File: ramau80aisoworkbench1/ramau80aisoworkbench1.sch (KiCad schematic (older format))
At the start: 190 parts, among them SW1 SW_PUSH, U1 ATmega32U4-AU, Y1 16MHz

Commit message: label updates
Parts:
- gave numbers to parts that had none: 13
- renumbered C6 to C1, C5 to C2, C4 to C3, C1 to C4, C2 to C5, C3 to C6, D_BKSP to D_BKSP1, D_EQ to D_EQ1, D_MIN to D_MIN1, MX_BKSP to MX_BKSP1, MX_EQ to MX_EQ1, MX_MIN to MX_MIN1
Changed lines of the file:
@@
 $EndComp
 $Comp
-L Device:C_Small C6
+L Device:C_Small C1
 U 1 1 6413AAB8
 P 2700 5600
-F 0 "C6" H 2792 5646 50  0000 L CNN
+F 0 "C1" H 2792 5646 50  0000 L CNN
 F 1 "C_Small" H 2792 5555 50  0000 L CNN
 F 2 "Capacitor_SMD:C_0805_2012Metric" H 2700 5600 50  0001 C CNN
@@
 	3650 5750 3650 5550
 $Comp
-L Device:C_Small C4
+L Device:C_Small C3
 U 1 1 64154BDF
 P 4000 5250
-F 0 "C4" V 3771 5250 50  0000 C CNN
+F 0 "C3" V 3771 5250 50  0000 C CNN
 F 1 "22pF" V 3862 5250 50  0000 C CNN
 F 2 "Capacitor_SMD:C_0805_2012Metric" H 4000 5250 50  0001 C CNN
@@
 $EndComp
 $Comp
-L Device:C_Small C5
+L Device:C_Small C2
 U 1 1 6415BB1E
 P 3650 5250
-F 0 "C5" V 3421 5250 50  0000 C CNN
+F 0 "C2" V 3421 5250 50  0000 C CNN
 F 1 "22pF" V 3512 5250 50  0000 C CNN
 F 2 "Capacitor_SMD:C_0805_2012Metric" H 3650 5250 50  0001 C CNN
@@
 $EndComp
 $Comp
-L Device:D_Small D_F?
+L Device:D_Small D_F13
 U 1 1 641E009B
 P 8750 1450
-F 0 "D_F?" V 8796 1380 50  0000 R CNN
+F 0 "D_F13" V 8796 1380 50  0000 R CNN
 F 1 "D_Small" V 8705 1380 50  0000 R CNN
 F 2 "Diode_SMD:D_SOD-123" V 8750 1450 50  0001 C CNN
@@
 $EndComp
 $Comp
-L Device:D_Small D_F?
+L Device:D_Small D_F14
 U 1 1 641E0688
 P 9250 1450
-F 0 "D_F?" V 9296 1380 50  0000 R CNN
+F 0 "D_F14" V 9296 1380 50  0000 R CNN
 F 1 "D_Small" V 9205 1380 50  0000 R CNN
 F 2 "Diode_SMD:D_SOD-123" V 9250 1450 50  0001 C CNN
@@
 $EndComp
 $Comp
-L Device:D_Small D_F?
+L Device:D_Small D_F15
 U 1 1 641E0B3F
 P 9750 1450
-F 0 "D_F?" V 9796 1380 50  0000 R CNN
+F 0 "D_F15" V 9796 1380 50  0000 R CNN
 F 1 "D_Small" V 9705 1380 50  0000 R CNN
 F 2 "Diode_SMD:D_SOD-123" V 9750 1450 50  0001 C CNN
@@
 Wire Wire Line
 	1250 1950 1450 1950
-$Comp
-L MX_Alps_Hybrid:MX-NoLED MX_GRV
-U 1 1 64185B4E
-P 1500 1800
-F 0 "MX_GRV" H 1533 2023 60  0000 C CNN
-F 1 "MX-NoLED" H 1533 1949 20  0000 C CNN
-F 2 "MX_Only:MXOnly-1U" H 875 1775 60  0001 C CNN
-F 3 "" H 875 1775 60  0001 C CNN
-	1    1500 1800
-	1    0    0    -1
-$EndComp
 Wire Wire Line
 	1650 1150 1650 900
@@
 $EndComp
 $Comp
-L MX_Alps_Hybrid:MX-NoLED MX_MIN
+L MX_Alps_Hybrid:MX-NoLED MX_MIN1
 U 1 1 642DE91B
 P 7000 1800
-F 0 "MX_MIN" H 7033 2023 60  0000 C CNN
+F 0 "MX_MIN1" H 7033 2023 60  0000 C CNN
 F 1 "MX-NoLED" H 7033 1949 20  0000 C CNN
 F 2 "MX_Only:MXOnly-1U" H 6375 1775 60  0001 C CNN
@@
 $EndComp
 $Comp
-L MX_Alps_Hybrid:MX-NoLED MX_EQ
+L MX_Alps_Hybrid:MX-NoLED MX_EQ1
 U 1 1 642DE925
 P 7500 1800
-F 0 "MX_EQ" H 7533 2023 60  0000 C CNN
+F 0 "MX_EQ1" H 7533 2023 60  0000 C CNN
 F 1 "MX-NoLED" H 7533 1949 20  0000 C CNN
 F 2 "MX_Only:MXOnly-1U" H 6875 1775 60  0001 C CNN
@@
 $EndComp
 $Comp
-L MX_Alps_Hybrid:MX-NoLED MX_BKSP
+L MX_Alps_Hybrid:MX-NoLED MX_BKSP1
 U 1 1 642DE92F
 P 8100 1800
-F 0 "MX_BKSP" H 8133 2023 60  0000 C CNN
+F 0 "MX_BKSP1" H 8133 2023 60  0000 C CNN
 F 1 "MX-NoLED" H 8133 1949 20  0000 C CNN
 F 2 "MX_Only:MXOnly-1U" H 7475 1775 60  0001 C CNN
@@
 $EndComp
 $Comp
-L Device:D_Small D_MIN
+L Device:D_Small D_MIN1
 U 1 1 642DE99D
 P 6750 2050
-F 0 "D_MIN" V 6796 1980 50  0000 R CNN
+F 0 "D_MIN1" V 6796 1980 50  0000 R CNN
 F 1 "D_Small" V 6705 1980 50  0000 R CNN
 F 2 "Diode_SMD:D_SOD-123" V 6750 2050 50  0001 C CNN
@@
 $EndComp
 $Comp
-L Device:D_Small D_EQ
+L Device:D_Small D_EQ1
 U 1 1 642DE9A7
 P 7250 2050
-F 0 "D_EQ" V 7296 1980 50  0000 R CNN
+F 0 "D_EQ1" V 7296 1980 50  0000 R CNN
 F 1 "D_Small" V 7205 1980 50  0000 R CNN
 F 2 "Diode_SMD:D_SOD-123" V 7250 2050 50  0001 C CNN
@@
 $EndComp
 $Comp
-L Device:D_Small D_BKSP
+L Device:D_Small D_BKSP1
 U 1 1 642DE9B1
 P 7850 2050
-F 0 "D_BKSP" V 7896 1980 50  0000 R CNN
+F 0 "D_BKSP1" V 7896 1980 50  0000 R CNN
 F 1 "D_Small" V 7805 1980 50  0000 R CNN
 F 2 "Diode_SMD:D_SOD-123" V 7850 2050 50  0001 C CNN
@@
 	2750 1350 2950 1350
 $Comp
-L Device:D_Small D_F?
+L Device:D_Small D_F12
 U 1 1 641DF7DE
 P 8100 1450
-F 0 "D_F?" V 8146 1380 50  0000 R CNN
+F 0 "D_F12" V 8146 1380 50  0000 R CNN
 F 1 "D_Small" V 8055 1380 50  0000 R CNN
 F 2 "Diode_SMD:D_SOD-123" V 8100 1450 50  0001 C CNN
@@
 $EndComp
 $Comp
-L Device:D_Small D_F?
+L Device:D_Small D_F11
 U 1 1 641DEF62
 P 7600 1450
-F 0 "D_F?" V 7646 1380 50  0000 R CNN
+F 0 "D_F11" V 7646 1380 50  0000 R CNN
 F 1 "D_Small" V 7555 1380 50  0000 R CNN
 F 2 "Diode_SMD:D_SOD-123" V 7600 1450 50  0001 C CNN
@@
 $EndComp
 $Comp
-L Device:D_Small D_F?
+L Device:D_Small D_F10
 U 1 1 641DE754
 P 7100 1450
-F 0 "D_F?" V 7146 1380 50  0000 R CNN
+F 0 "D_F10" V 7146 1380 50  0000 R CNN
 F 1 "D_Small" V 7055 1380 50  0000 R CNN
 F 2 "Diode_SMD:D_SOD-123" V 7100 1450 50  0001 C CNN
@@
 $EndComp
 $Comp
-L Device:D_Small D_F?
+L Device:D_Small D_F9
 U 1 1 641DDFBE
 P 6600 1450
-F 0 "D_F?" V 6646 1380 50  0000 R CNN
+F 0 "D_F9" V 6646 1380 50  0000 R CNN
 F 1 "D_Small" V 6555 1380 50  0000 R CNN
 F 2 "Diode_SMD:D_SOD-123" V 6600 1450 50  0001 C CNN
@@
 $EndComp
 $Comp
-L Device:D_Small D_F?
+L Device:D_Small D_F8
 U 1 1 641D8A59
 P 6050 1450
-F 0 "D_F?" V 6096 1380 50  0000 R CNN
+F 0 "D_F8" V 6096 1380 50  0000 R CNN
 F 1 "D_Small" V 6005 1380 50  0000 R CNN
 F 2 "Diode_SMD:D_SOD-123" V 6050 1450 50  0001 C CNN
@@
 $EndComp
 $Comp
-L Device:D_Small D_F?
+L Device:D_Small D_F7
 U 1 1 641D8115
 P 5550 1450
-F 0 "D_F?" V 5596 1380 50  0000 R CNN
+F 0 "D_F7" V 5596 1380 50  0000 R CNN
 F 1 "D_Small" V 5505 1380 50  0000 R CNN
 F 2 "Diode_SMD:D_SOD-123" V 5550 1450 50  0001 C CNN
@@
 $EndComp
 $Comp
-L Device:D_Small D_F?
+L Device:D_Small D_F6
 U 1 1 641D79ED
 P 5050 1450
-F 0 "D_F?" V 5096 1380 50  0000 R CNN
+F 0 "D_F6" V 5096 1380 50  0000 R CNN
 F 1 "D_Small" V 5005 1380 50  0000 R CNN
 F 2 "Diode_SMD:D_SOD-123" V 5050 1450 50  0001 C CNN
@@
 $EndComp
 $Comp
-L Device:D_Small D_F?
+L Device:D_Small D_F5
 U 1 1 641D7374
 P 4550 1450
-F 0 "D_F?" V 4596 1380 50  0000 R CNN
+F 0 "D_F5" V 4596 1380 50  0000 R CNN
 F 1 "D_Small" V 4505 1380 50  0000 R CNN
 F 2 "Diode_SMD:D_SOD-123" V 4550 1450 50  0001 C CNN
@@
 $EndComp
 $Comp
-L Device:D_Small D_F?
+L Device:D_Small D_F4
 U 1 1 641D6AE4
 P 3750 1450
-F 0 "D_F?" V 3796 1380 50  0000 R CNN
+F 0 "D_F4" V 3796 1380 50  0000 R CNN
 F 1 "D_Small" V 3705 1380 50  0000 R CNN
 F 2 "Diode_SMD:D_SOD-123" V 3750 1450 50  0001 C CNN
@@
 $EndComp
 $Comp
-L Device:D_Small D_F?
+L Device:D_Small D_F3
 U 1 1 641D648E
 P 3250 1450
-F 0 "D_F?" V 3296 1380 50  0000 R CNN
+F 0 "D_F3" V 3296 1380 50  0000 R CNN
 F 1 "D_Small" V 3205 1380 50  0000 R CNN
 F 2 "Diode_SMD:D_SOD-123" V 3250 1450 50  0001 C CNN
@@
 Wire Wire Line
 	1950 2750 2450 2750
-Wire Wire Line
-	1650 1150 1650 1750
 Connection ~ 1650 1150
 Wire Wire Line
@@
 	9650 900  9650 1150
 Wire Wire Line
-	1650 1750 1650 2250
-Wire Wire Line
 	1650 2250 1850 2250
 Wire Wire Line
 	1850 2250 1850 2350
-Connection ~ 1650 1750
 Wire Wire Line
 	1850 2950 1900 2950
@@
 Connection ~ 7050 4900
 $Comp
-L Device:D_Small D_RIGHT
-U 1 1 645C385A
-P 9750 4800
-F 0 "D_RIGHT" V 9796 4730 50  0000 R CNN
-F 1 "D_Small" V 9705 4730 50  0000 R CNN
-F 2 "Diode_SMD:D_SOD-123" V 9750 4800 50  0001 C CNN
-F 3 "~" V 9750 4800 50  0001 C CNN
-	1    9750 4800
-	0    -1   -1   0
-$EndComp
-$Comp
-L Device:D_Small D_DOWN
-U 1 1 645C3850
-P 9250 4800
-F 0 "D_DOWN" V 9296 4730 50  0000 R CNN
-F 1 "D_Small" V 9205 4730 50  0000 R CNN
-F 2 "Diode_SMD:D_SOD-123" V 9250 4800 50  0001 C CNN
-F 3 "~" V 9250 4800 50  0001 C CNN
-	1    9250 4800
-	0    -1   -1   0
-$EndComp
-$Comp
-L Device:D_Small D_LEFT
-U 1 1 645C3846
-P 8750 4800
-F 0 "D_LEFT" V 8796 4730 50  0000 R CNN
-F 1 "D_Small" V 8705 4730 50  0000 R CNN
-F 2 "Diode_SMD:D_SOD-123" V 8750 4800 50  0001 C CNN
-F 3 "~" V 8750 4800 50  0001 C CNN
-	1    8750 4800
-	0    -1   -1   0
-$EndComp
-$Comp
 L Device:D_Small D_RCTRL
 U 1 1 645C383C
@@
 	8750 5950 9300 5950
 $Comp
-L Device:C_Small C1
+L Device:C_Small C4
 U 1 1 6414168B
 P 8750 6050
-F 0 "C1" H 8842 6096 50  0000 L CNN
+F 0 "C4" H 8842 6096 50  0000 L CNN
 F 1 "0.1uF" H 8842 6005 50  0000 L CNN
 F 2 "Capacitor_SMD:C_0805_2012Metric" H 8750 6050 50  0001 C CNN
@@
 $EndComp
 $Comp
-L Device:C_Small C2
+L Device:C_Small C5
 U 1 1 641400E1
 P 9300 6050
-F 0 "C2" H 9392 6096 50  0000 L CNN
+F 0 "C5" H 9392 6096 50  0000 L CNN
 F 1 "0.1uF" H 9392 6005 50  0000 L CNN
 F 2 "Capacitor_SMD:C_0805_2012Metric" H 9300 6050 50  0001 C CNN
@@
 $EndComp
 $Comp
-L Device:C_Small C3
+L Device:C_Small C6
 U 1 1 6413FCFD
 P 9800 6050
-F 0 "C3" H 9892 6096 50  0000 L CNN
+F 0 "C6" H 9892 6096 50  0000 L CNN
 F 1 "0.1uF" H 9892 6005 50  0000 L CNN
 F 2 "Capacitor_SMD:C_0805_2012Metric" H 9800 6050 50  0001 C CNN
@@
 Wire Wire Line
 	4800 5550 4900 5550
+$Comp
+L Device:D_Small D_RIGHT
+U 1 1 645C385A
+P 9750 4800
+F 0 "D_RIGHT" V 9796 4730 50  0000 R CNN
+F 1 "D_Small" V 9705 4730 50  0000 R CNN
+F 2 "Diode_SMD:D_SOD-123" V 9750 4800 50  0001 C CNN
+F 3 "~" V 9750 4800 50  0001 C CNN
+	1    9750 4800
+	0    -1   -1   0
+$EndComp
+$Comp
+L Device:D_Small D_DOWN
+U 1 1 645C3850
+P 9250 4800
+F 0 "D_DOWN" V 9296 4730 50  0000 R CNN
+F 1 "D_Small" V 9205 4730 50  0000 R CNN
+F 2 "Diode_SMD:D_SOD-123" V 9250 4800 50  0001 C CNN
+F 3 "~" V 9250 4800 50  0001 C CNN
+	1    9250 4800
+	0    -1   -1   0
+$EndComp
+$Comp
+L Device:D_Small D_LEFT
+U 1 1 645C3846
+P 8750 4800
+F 0 "D_LEFT" V 8796 4730 50  0000 R CNN
+F 1 "D_Small" V 8705 4730 50  0000 R CNN
+F 2 "Diode_SMD:D_SOD-123" V 8750 4800 50  0001 C CNN
+F 3 "~" V 8750 4800 50  0001 C CNN
+	1    8750 4800
+	0    -1   -1   0
+$EndComp
+Connection ~ 1650 1750
+Wire Wire Line
+	1650 1750 1650 2250
+Wire Wire Line
+	1650 1150 1650 1750
+$Comp
+L MX_Alps_Hybrid:MX-NoLED MX_GRV
+U 1 1 64185B4E
+P 1500 1800
+F 0 "MX_GRV" H 1533 2023 60  0000 C CNN
+F 1 "MX-NoLED" H 1533 1949 20  0000 C CNN
+F 2 "MX_Only:MXOnly-1U" H 875 1775 60  0001 C CNN
+F 3 "" H 875 1775 60  0001 C CNN
+	1    1500 1800
+	1    0    0    -1
+$EndComp
 $EndSCHEMATC

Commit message: label updates
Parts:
- renumbered D_A to D_A100, D_B to D_B100, D_BKSP1 to D_BKSP100, D_C to D_C100, D_CAPS to D_CAPS100, D_COM to D_COM100, D_D to D_D100, D_DEL to D_DEL100, D_DOWN to D_DOWN100, D_E to D_E100, D_END to D_END100, D_ENT to D_ENT100, D_EQ1 to D_EQ100, D_ESC to D_ESC100, D_F to D_F100, D_FN to D_FN100, D_G to D_G100, D_GRV to D_GRV100, D_H to D_H100, D_HOME to D_HOME100, D_I to D_I100, D_J to D_J100, D_K to D_K100, D_L to D_L100, D_LALT to D_LALT100, D_LCTRL to D_LCTRL100, D_LEFT to D_LEFT100, D_LOS to D_LOS100, D_LSFT to D_LSFT100, D_LSQ to D_LSQ100, D_M to D_M100, D_MIN1 to D_MIN100, D_N to D_N100, D_O to D_O100, D_P to D_P100, D_PER to D_PER100, D_PGDN to D_PGDN100, D_PGUP to D_PGUP100, D_PIPE to D_PIPE100, D_Q to D_Q100, D_QUO to D_QUO100, D_R to D_R100, D_RALT to D_RALT100, D_RCTRL to D_RCTRL100, D_RIGHT to D_RIGHT100, D_ROS to D_ROS100, D_RSFT to D_RSFT100, D_RSQ to D_RSQ100, D_S to D_S100, D_SEMI to D_SEMI100, D_SLASH to D_SLASH100, D_SPACE to D_SPACE100, D_T to D_T100, D_TAB to D_TAB100, D_TILD to D_TILD100, D_U to D_U100, D_UP to D_UP100, D_V to D_V100, D_W to D_W100, D_X to D_X100, D_Y to D_Y100, D_Z to D_Z100, MX_A to MX_A100, MX_B to MX_B100, MX_BKSP1 to MX_BKSP100, MX_C to MX_C100, MX_CAPS to MX_CAPS100, MX_COM to MX_COM100, MX_D to MX_D100, MX_DEL to MX_DEL100, MX_DOWN to MX_DOWN100, MX_E to MX_E100, MX_END to MX_END100, MX_ENT to MX_ENT100, MX_EQ1 to MX_EQ100, MX_ESC to MX_ESC100, MX_F to MX_F100, MX_FN to MX_FN100, MX_G to MX_G100, MX_GRV to MX_GRV100, MX_H to MX_H100, MX_HOME to MX_HOME100, MX_I to MX_I100, MX_J to MX_J100, MX_K to MX_K100, MX_L to MX_L100, MX_LALT to MX_LALT100, MX_LCTRL to MX_LCTRL100, MX_LEFT to MX_LEFT100, MX_LOS to MX_LOS100, MX_LSFT to MX_LSFT100, MX_LSQ to MX_LSQ100, MX_M to MX_M100, MX_MIN1 to MX_MIN100, MX_N to MX_N100, MX_O to MX_O100, MX_P to MX_P100, MX_PER to MX_PER100, MX_PGDN to MX_PGDN100, MX_PGUP to MX_PGUP100, MX_PIPE to MX_PIPE100, MX_Q to MX_Q100, MX_QUO to MX_QUO100, MX_R to MX_R100, MX_RALT to MX_RALT100, MX_RCTRL to MX_RCTRL100, MX_RIGHT to MX_RIGHT100, MX_ROS to MX_ROS100, MX_RSFT to MX_RSFT100, MX_RSQ to MX_RSQ100, MX_S to MX_S100, MX_SEMI to MX_SEMI100, MX_SLASH to MX_SLASH100, MX_SPACE to MX_SPACE100, MX_T to MX_T100, MX_TAB to MX_TAB100, MX_TILD to MX_TILD100, MX_U to MX_U100, MX_UP to MX_UP100, MX_V to MX_V100, MX_W to MX_W100, MX_X to MX_X100, MX_Y to MX_Y100, MX_Z to MX_Z100

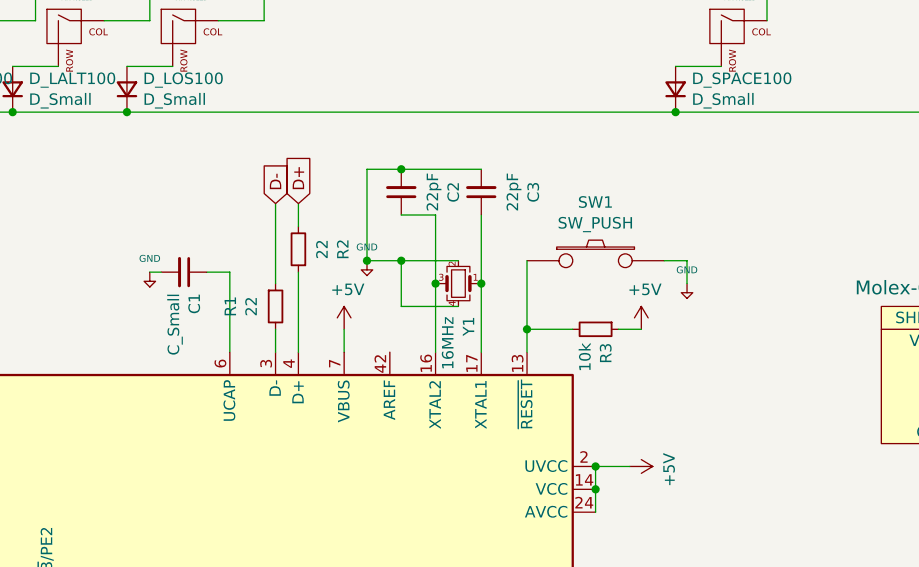
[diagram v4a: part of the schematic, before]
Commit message: fixed error in footprint assignment. updated switch footprints to use appropriate size, ditched leds
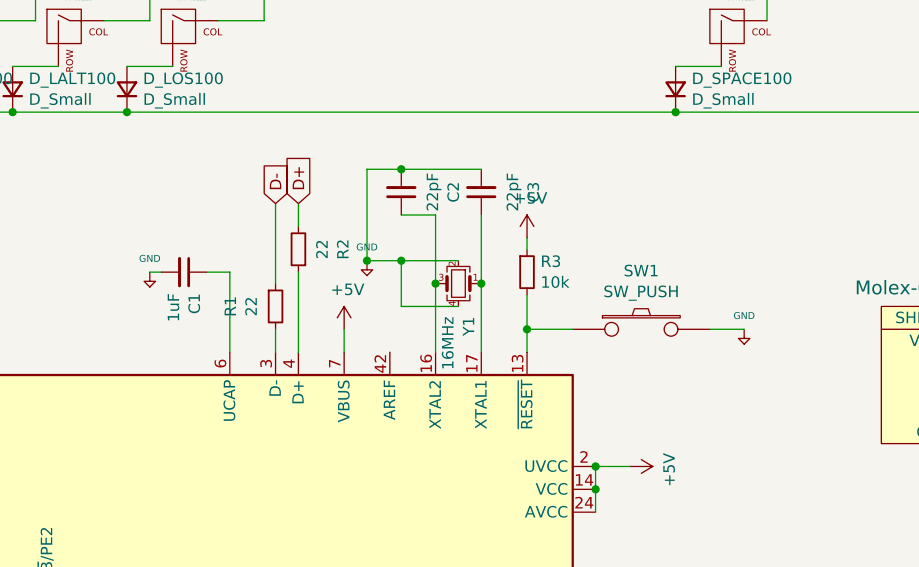
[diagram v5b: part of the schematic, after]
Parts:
- C1: value C_Small -> 1uF
- MX_A100, MX_B100, MX_C100, MX_COM100, MX_D100, MX_DEL100, MX_DOWN100, MX_E100, MX_END100, MX_EQ100, MX_ESC100, MX_F1, MX_F10, MX_F100, MX_F11, MX_F12, MX_F13, MX_F14, MX_F15, MX_F2, MX_F3, MX_F4, MX_F5, MX_F6, MX_F7, MX_F8, MX_F9, MX_FN100, MX_G100, MX_GRV100, MX_H100, MX_HOME100, MX_I100, MX_J100, MX_K100, MX_L100, MX_LALT100, MX_LEFT100, MX_LSQ100, MX_M100, MX_MIN100, MX_N0, MX_N1, MX_N100, MX_N2, MX_N3, MX_N4, MX_N5, MX_N6, MX_N7, MX_N8, MX_N9, MX_O100, MX_P100, MX_PER100, MX_PGDN100, MX_PGUP100, MX_PIPE100, MX_Q100, MX_QUO100, MX_R100, MX_RALT100, MX_RIGHT100, MX_RSQ100, MX_S100, MX_SEMI100, MX_SLASH100, MX_T100, MX_TILD100, MX_U100, MX_UP100, MX_V100, MX_W100, MX_X100, MX_Y100, MX_Z100: footprint MX_Only:MXOnly-1U -> MX_Only:MXOnly-1U-NoLED
- MX_BKSP100: footprint MX_Only:MXOnly-1U -> MX_Only:MXOnly-2U-NoLED
- MX_CAPS100: footprint MX_Only:MXOnly-1U -> MX_Only:MXOnly-1.75U-NoLED
- MX_ENT100: footprint MX_Only:MXOnly-1U -> MX_Only:MXOnly-ISO-ROTATED-NoLED
- MX_LCTRL100, MX_LOS100, MX_RCTRL100, MX_ROS100, MX_TAB100: footprint MX_Only:MXOnly-1U -> MX_Only:MXOnly-1.5U-NoLED
- MX_LSFT100: footprint MX_Only:MXOnly-1U -> MX_Only:MXOnly-1.25U-NoLED
- MX_RSFT100: footprint MX_Only:MXOnly-1U -> MX_Only:MXOnly-2.75U-NoLED
- MX_SPACE100: footprint MX_Only:MXOnly-1U -> MX_Only:MXOnly-7U-NoLED
- USB1: footprint random-keyboard-parts:PJ-3200B-4A-Assembly -> random-keyboard-parts:Molex-0548190589
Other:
- moved on the sheet: R3, SW1
